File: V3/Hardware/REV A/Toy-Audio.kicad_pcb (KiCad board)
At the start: 2 copper layers, 24 x 14 mm, 26 parts, among them J1 CONN_01X02, J2 CONN_01X04, J3 CONN_01X03, J4 CONN_01X03, J5 CONN_01X04, U1 XC6206P332MR, U2 STM32F030F4P6, U3 W25Q32FVSIG, U4 TS4890, U5 MCP48FEB02-E/UN

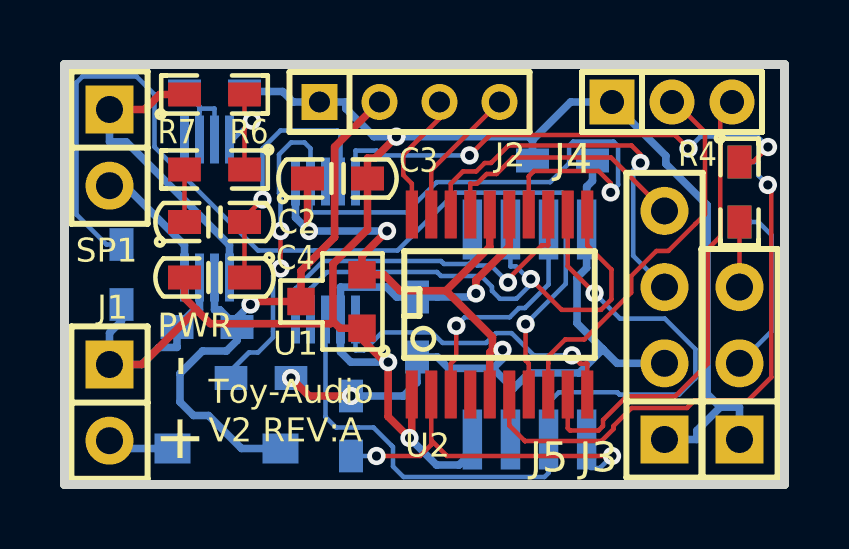
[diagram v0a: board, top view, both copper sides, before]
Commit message: Improved Wake-up pin stability WKUP1. modiefied schematic files. Software V1 is compatible with hardware V2
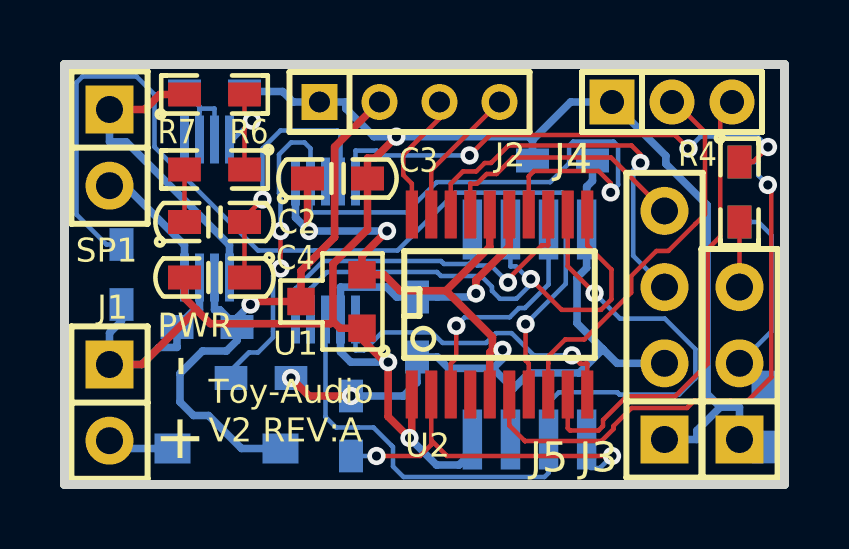
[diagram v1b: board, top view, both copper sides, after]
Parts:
- added R5: 10k, MvdL:R0603, B.Cu at (119.3, 100.8)
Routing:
- net GND: track 76.7 -> 78.5 mm
- net Net-(J3-Pad2): track 5.96 -> 7.09 mm
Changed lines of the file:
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@@
 (kicad_pcb (version 4) (host pcbnew 4.0.0-rc2-stable)
   (general
-    (links 67)
+    (links 69)
     (no_connects 0)
     (area 95.849999 88.849999 120.150001 103.150001)
     (thickness 1.6)
     (drawings 8)
-    (tracks 445)
+    (tracks 450)
     (zones 0)
-    (modules 26)
+    (modules 27)
     (nets 29)
   )
@@
     )
   )
+  (module MvdL:R0603 (layer B.Cu)
+    (at 119.3 100.75 270)
+    (attr smd)
+    (fp_text reference R5 (at -3 -0.15 540) (layer B.SilkS)
+      (effects (font (size 0.8128 0.7112) (thickness 0.1524)) (justify mirror))
+    )
+    (fp_text value 10k (at 0.0254 -1.143 270) (layer B.Fab)
+      (effects (font (size 0.50038 0.50038) (thickness 0.10922)) (justify mirror))
+    )
+    (fp_line (start -1.6002 0.635) (end -1.7272 0.635) (layer B.SilkS) (width 0.1524))
+    (fp_line (start -1.7772 0.635) (end -1.7772 -0.635) (layer B.SilkS) (width 0.1524))
+    (fp_line (start -1.7272 -0.635) (end -1.6256 -0.635) (layer B.SilkS) (width 0.1524))
+    (fp_line (start 1.6002 0.635) (end 1.7272 0.635) (layer B.SilkS) (width 0.1524))
+    (fp_line (start 1.7772 0.635) (end 1.7772 -0.635) (layer B.SilkS) (width 0.1524))
+    (fp_line (start 1.7272 -0.635) (end 1.6002 -0.635) (layer B.SilkS) (width 0.1524))
+    (fp_line (start 0.5814 0.635) (end 1.7752 0.635) (layer B.SilkS) (width 0.1524))
+    (fp_line (start 0.5814 -0.635) (end 1.7752 -0.635) (layer B.SilkS) (width 0.1524))
+    (fp_line (start -0.5564 -0.635) (end -1.7502 -0.635) (layer B.SilkS) (width 0.1524))
+    (fp_line (start -0.5814 0.635) (end -1.7752 0.635) (layer B.SilkS) (width 0.1524))
+    (fp_circle (center -1.7974 -0.658) (end -1.7974 -0.531) (layer B.SilkS) (width 0.1524))
+    (pad 1 smd rect (at -1 0 270) (size 1.0922 0.8) (layers B.Cu B.Paste B.Mask)
+      (net 15 "Net-(J3-Pad2)") (clearance 0.1524))
+    (pad 2 smd rect (at 1 0 270) (size 1.0922 0.8) (layers B.Cu B.Paste B.Mask)
+      (net 1 GND) (clearance 0.1524))
+    (model smd/chip_cms.wrl
+      (at (xyz 0 0 0))
+      (scale (xyz 0.1 0.1 0.1))
+      (rotate (xyz 0 0 0))
+    )
+  )
   (gr_text - (at 99.75 99.05 90) (layer F.SilkS)
     (effects (font (size 1.5 1.5) (thickness 0.3)))
@@
     (effects (font (size 1.5 1.5) (thickness 0.3)))
   )
+  (segment (start 118.5 101.5) (end 119.05 101.5) (width 0.254) (layer B.Cu) (net 1) (status C00000))
+  (segment (start 119.05 101.5) (end 119.3 101.75) (width 0.254) (layer B.Cu) (net 1) (status C00000))
+  (segment (start 119.3 101.75) (end 118.5 101.5) (width 0.254) (layer B.Cu) (net 1) (status C00000))
   (segment (start 97.9 97) (end 97.9 97.55) (width 0.254) (layer B.Cu) (net 1))
   (segment (start 97.5 97.95) (end 97.5 99) (width 0.254) (layer B.Cu) (net 1))
@@
   (segment (start 102 94.25) (end 102 94.8789) (width 0.1524) (layer F.Cu) (net 14))
   (segment (start 102 94.8789) (end 102 96.1) (width 0.1524) (layer F.Cu) (net 14))
+  (segment (start 118.5 98.96) (end 118.51 98.96) (width 0.1524) (layer B.Cu) (net 15) (status C00000))
+  (segment (start 118.51 98.96) (end 119.3 99.75) (width 0.1524) (layer B.Cu) (net 15) (status C00000))
   (segment (start 119.5697 94.6908) (end 119.1289 94.25) (width 0.1524) (layer B.Cu) (net 15))
   (segment (start 119.5697 97.8903) (end 119.5697 94.6908) (width 0.1524) (layer B.Cu) (net 15))
